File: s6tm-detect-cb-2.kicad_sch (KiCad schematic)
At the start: 51 parts, among them J1 USB_C_Receptacle_USB2.0_14P, J5 Conn_01x04_Pin, J8 Conn_01x04, SW1 SW_Push, SW2 SW_Push, SW3 SW_Push, U2 SN65HVD230, U3 ESP32-S3FN8, U7 NextPM, Y1 48M

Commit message: schem: add m3 mounting holes
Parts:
- added H5, H6, H7: MountingHole_Pad, MountingHole:MountingHole_3.2mm_M3_Pad_Via, symbol Mechanical:MountingHole_Pad
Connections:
- net GND: now also H5.1, H6.1, H7.1
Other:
- note added: "Mounting"

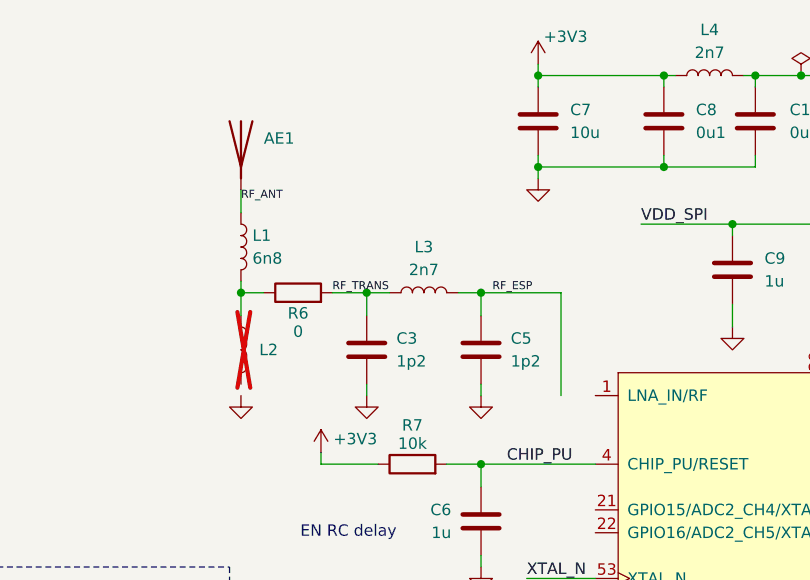
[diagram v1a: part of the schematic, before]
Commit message: schem: switch to external rf antenna
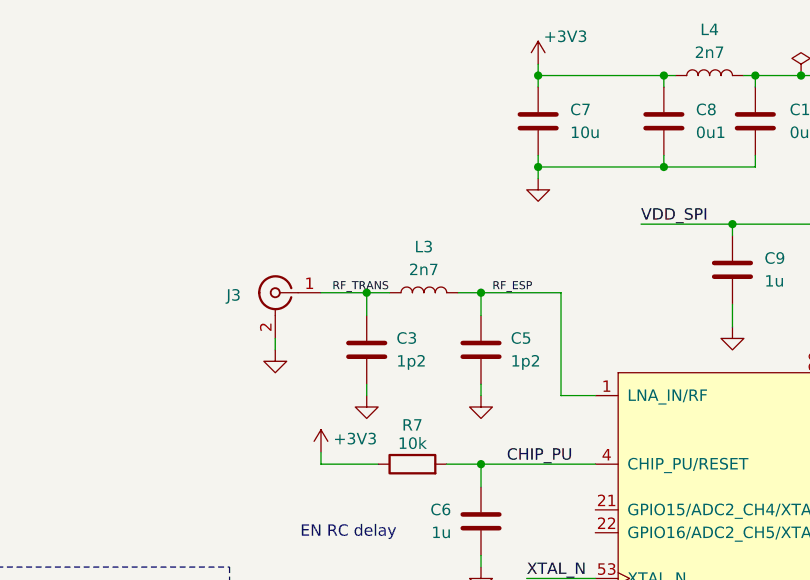
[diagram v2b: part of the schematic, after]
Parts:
- removed AE1: Antenna, RF_Antenna:Johanson_2450AT18x100, symbol Device:Antenna
- removed L1: 6n8, Inductor_SMD:L_0402_1005Metric, symbol Device:L
- removed L2: L, Inductor_SMD:L_0402_1005Metric, symbol Device:L
- removed R6: 0, Resistor_SMD:R_0402_1005Metric, symbol Device:R
- added J3: Conn_Coaxial, Connector_Coaxial:SMA_BAT_Wireless_BWSMA-KWE-Z001, symbol Connector:Conn_Coaxial
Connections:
- net GND: now also J3.2 (Ext)
- net RF_ESP: now also U3.1 (LNA_IN/RF)
- net RF_TRANS: now also J3.1 (In)

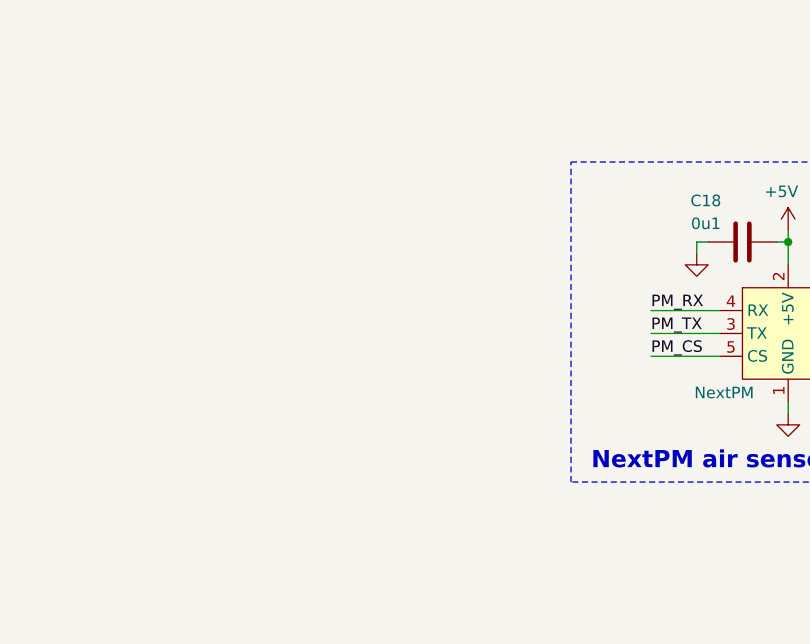
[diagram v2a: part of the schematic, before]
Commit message: schem: add htu21 h/t sensor
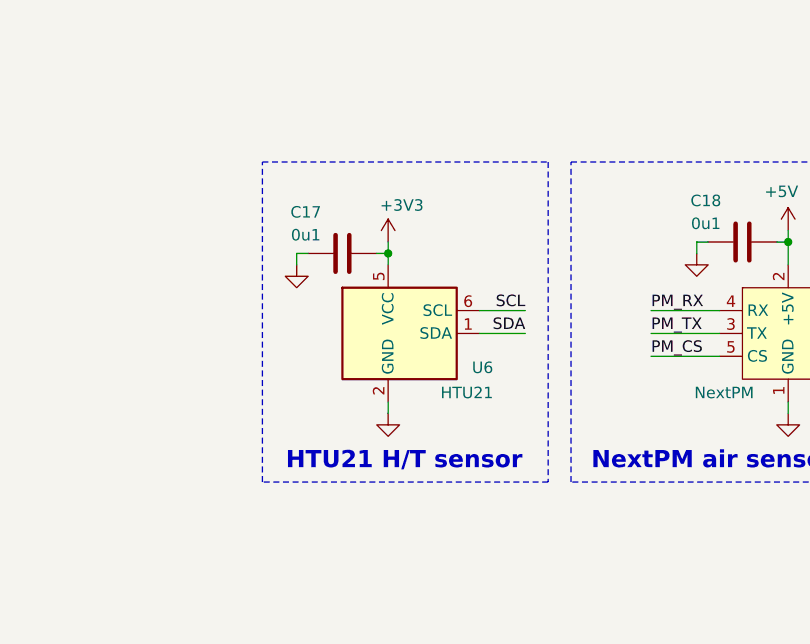
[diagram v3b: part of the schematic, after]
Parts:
- added C17: 0u1, Capacitor_SMD:C_0402_1005Metric, symbol Device:C
- added U6: HTU21, Package_SON:Texas_PWSON-N6, symbol Sensor_Humidity:HDC1080
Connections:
- net +3V3: now also C17.2, U6.5 (VCC)
- net GND: now also C17.1, U6.2 (GND)
- new net SCL: U6.6 (SCL)
- new net SDA: U6.1 (SDA)
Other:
- note added: "HTU21 H/T sensor"

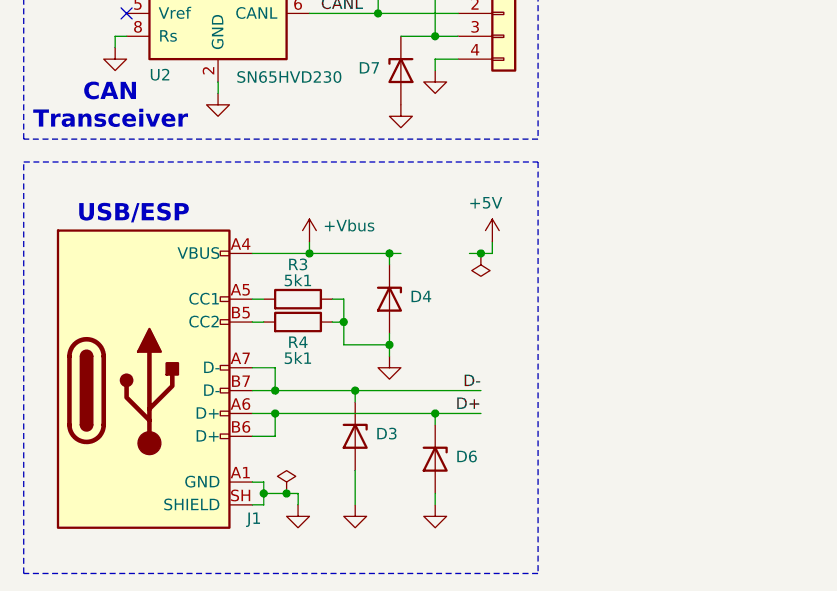
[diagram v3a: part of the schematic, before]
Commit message: schem: add MAX40203 ideal diode
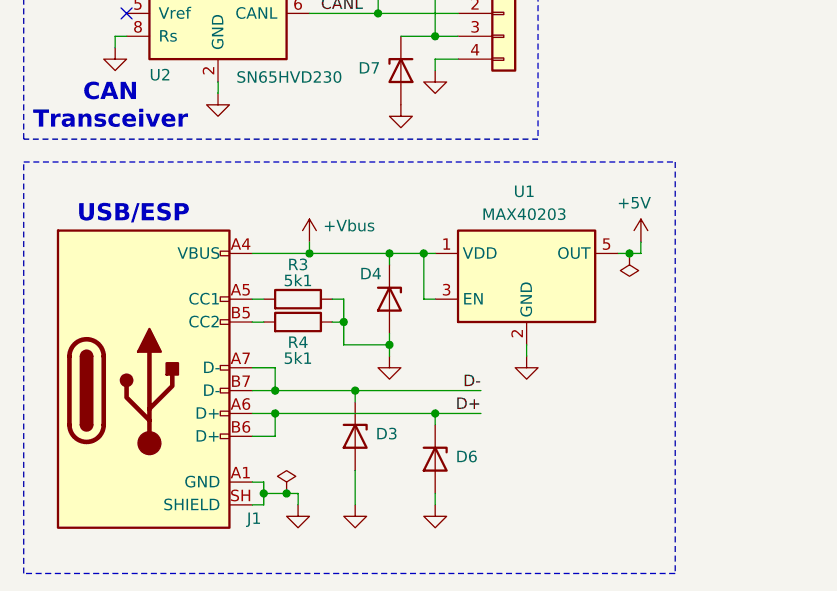
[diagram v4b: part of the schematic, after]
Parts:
- added U1: MAX40203, Package_TO_SOT_SMD:SOT-23-5, symbol Analog_Switch:MAX40200AUK
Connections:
- net +5V: now also U1.5 (OUT)
- net +Vbus: now also U1.1 (VDD), U1.3 (EN)
- net GND: now also U1.2 (GND)

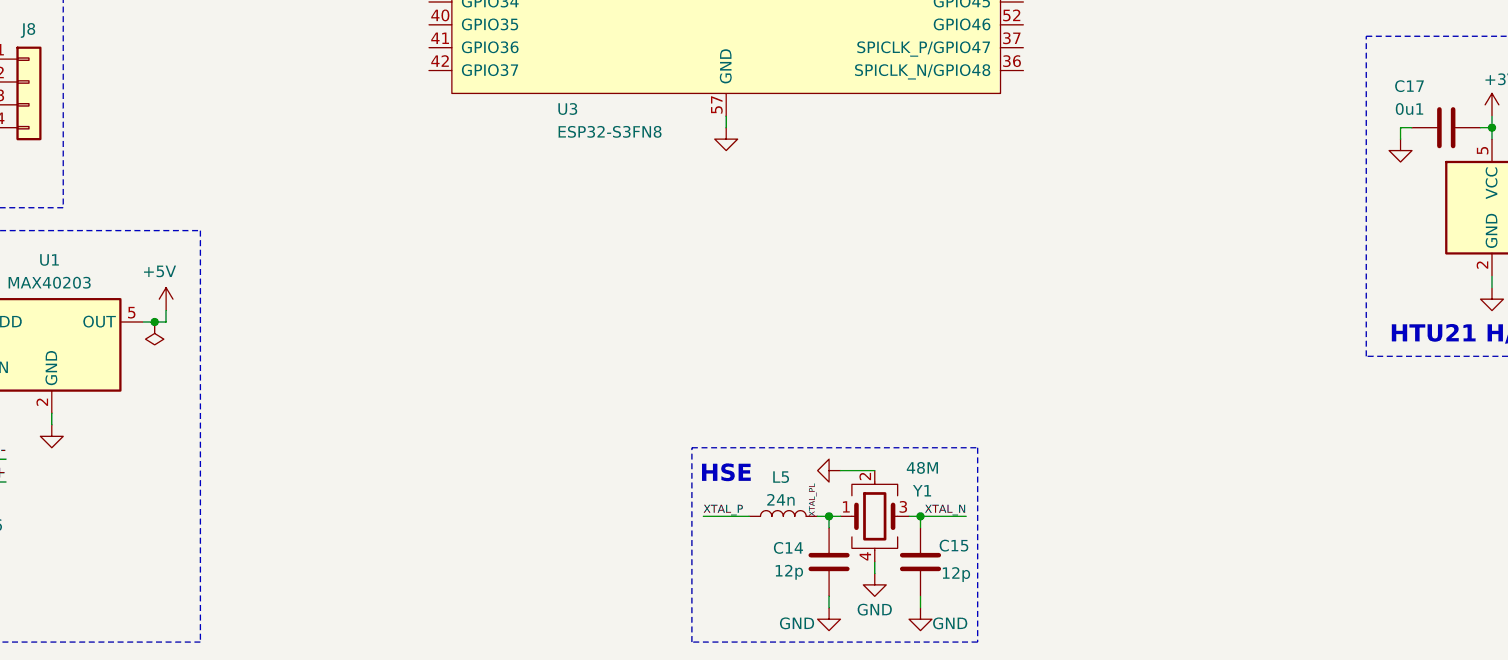
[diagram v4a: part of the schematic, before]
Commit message: schem: add TPS6282 3.3v SMPS
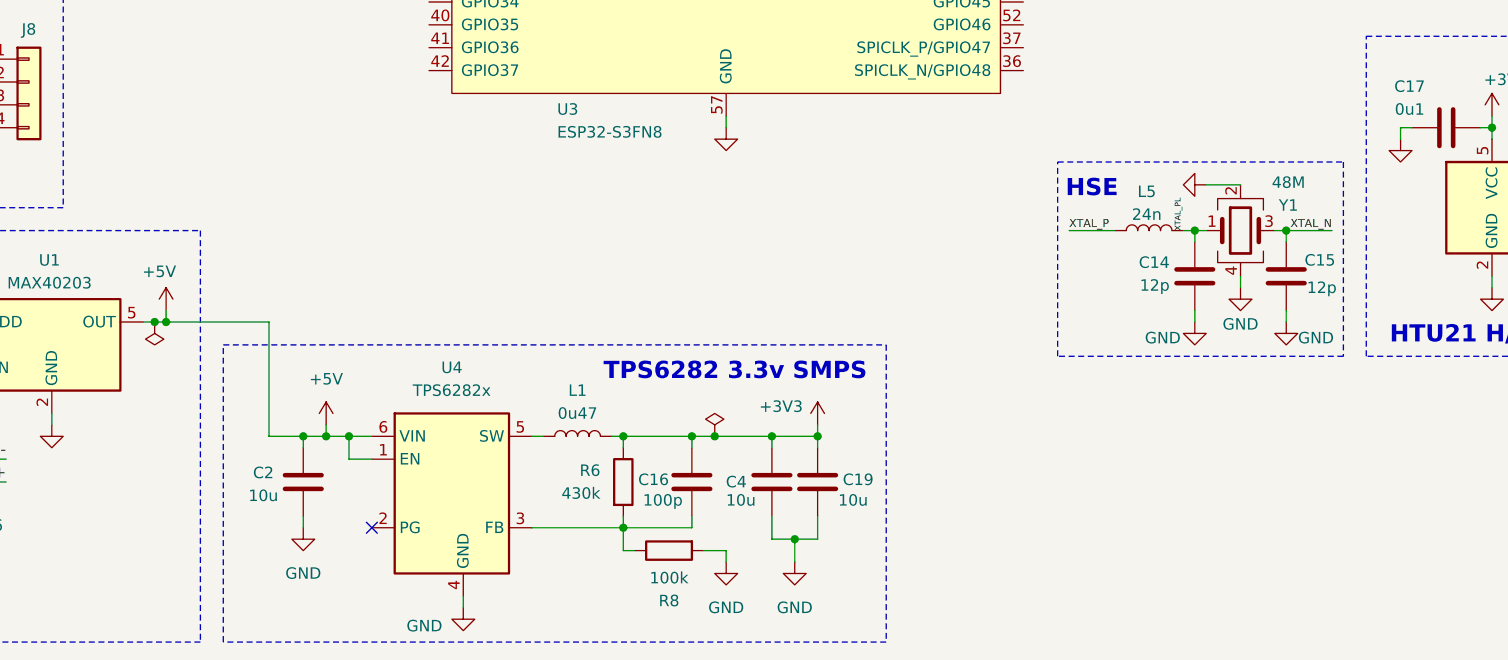
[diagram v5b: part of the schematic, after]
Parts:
- added C16: 100p, Capacitor_SMD:C_0402_1005Metric, symbol Device:C
- added C19, C4: 10u, Capacitor_SMD:C_0402_1005Metric, symbol Device:C
- added C2: 10u, Capacitor_SMD:C_0603_1608Metric, symbol Device:C
- added L1: 0u47, Pers:TDK_TFM201610ALC, symbol Device:L
- added R6: 430k, Resistor_SMD:R_0603_1608Metric, symbol Device:R
- added R8: 100k, Resistor_SMD:R_0402_1005Metric, symbol Device:R
- added U4: TPS6282x, Pers:Texas_VSON-6_1.5x1.5mm_P0.5mm_DMQ0006A, symbol Pers:TPS6282x
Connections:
- net +3V3: now also C16.1, C19.1, C4.1, L1.2, R6.1
- net +5V: now also C2.1, U4.1 (EN), U4.6 (VIN)
- net GND: now also C19.2, C2.2, C4.2, R8.2, U4.4 (GND)
- new net: C16.2, R6.2, R8.1, U4.3 (FB)
- new net: L1.1, U4.5 (SW)
- no-connect marks 2 -> 3
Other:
- note added: "TPS6282 3.3v SMPS"
- moved on the sheet: C14, C15, L5, Y1

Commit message: schem: update smps L part number
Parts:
- L1: JLCPCB Part # C2045043 -> C89446; Manufacturer Part Number TFM201610ALC-R47MTAA -> TFM201610GHM-R47MTAA
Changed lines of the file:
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@@
 			)
 		)
-		(property "JLCPCB Part #" "C2045043"
+		(property "JLCPCB Part #" "C89446"
 			(at 129.54 172.72 90)
 			(hide yes)
@@
 			)
 		)
-		(property "Manufacturer Part Number" "TFM201610ALC-R47MTAA"
+		(property "Manufacturer Part Number" "TFM201610GHM-R47MTAA"
 			(at 129.54 172.72 90)
 			(hide yes)

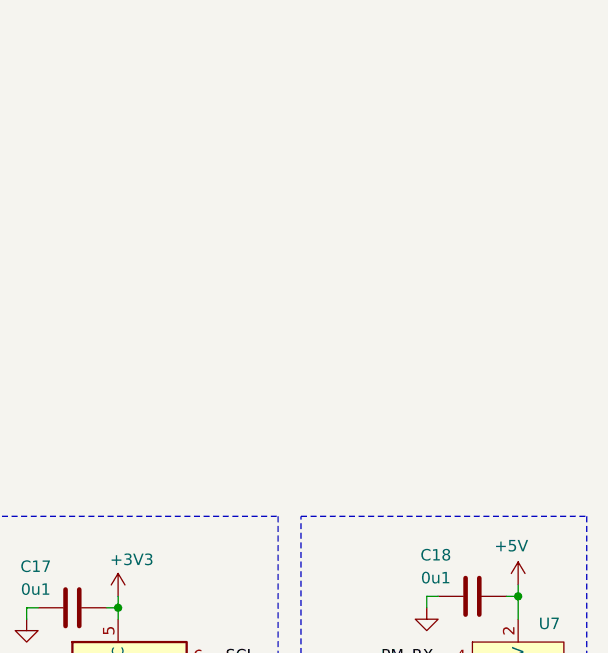
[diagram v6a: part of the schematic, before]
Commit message: schem: add ST7789 TFT connector
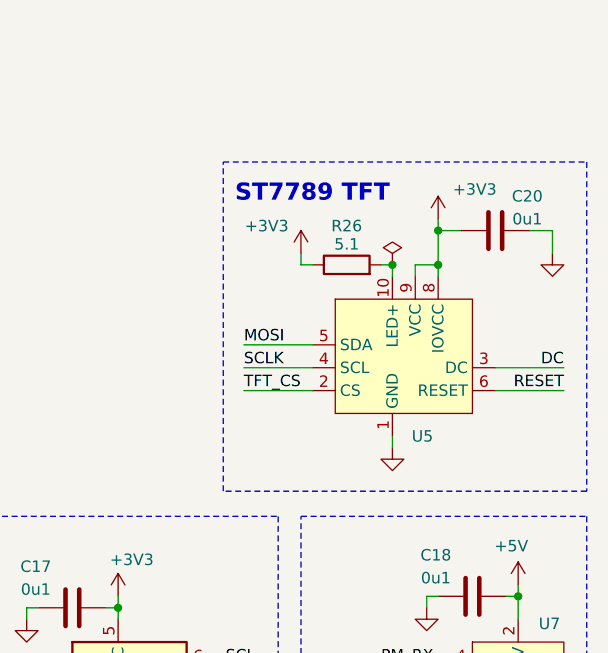
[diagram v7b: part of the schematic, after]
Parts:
- added C20: 0u1, Capacitor_SMD:C_0402_1005Metric, symbol Device:C
- added R26: 5.1, Resistor_SMD:R_0603_1608Metric, symbol Device:R
- added U5: (no value), Connector_FFC-FPC:Hirose_FH12-12S-0.5SH_1x12-1MP_P0.50mm_Horizontal, symbol GLCS:HS20HS072RX
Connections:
- net +3V3: now also C20.2, R26.1, U5.8 (IOVCC), U5.9 (VCC)
- net GND: now also C20.1, U5.1 (GND), U5.11 (LED-), U5.12 (GND), U5.MP (GND)
- new net: R26.2, U5.10 (LED+)
- new net DC: U5.3 (DC)
- new net MOSI: U5.5 (SDA)
- new net RESET: U5.6 (RESET)
- new net SCLK: U5.4 (SCL)
- new net TFT_CS: U5.2 (CS)
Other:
- note added: "ST7789 TFT"

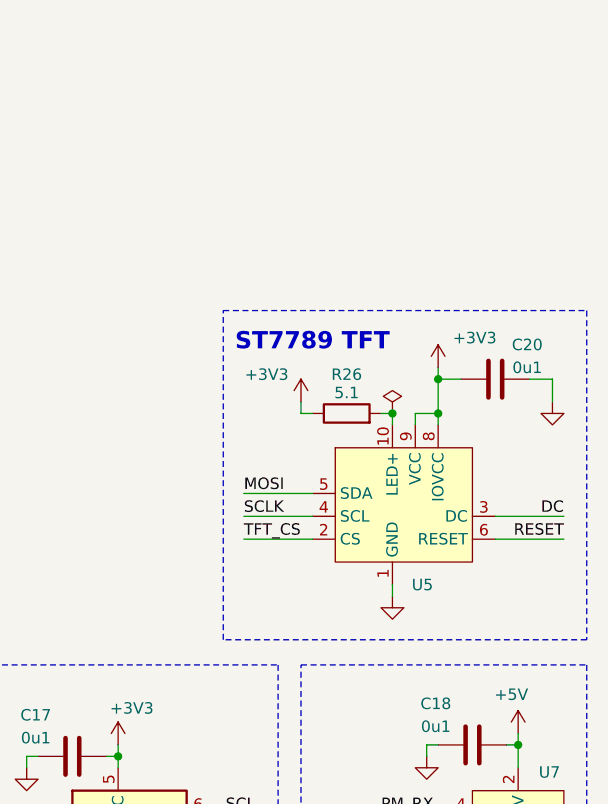
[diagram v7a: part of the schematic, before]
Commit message: schem: add tft dimming circuit
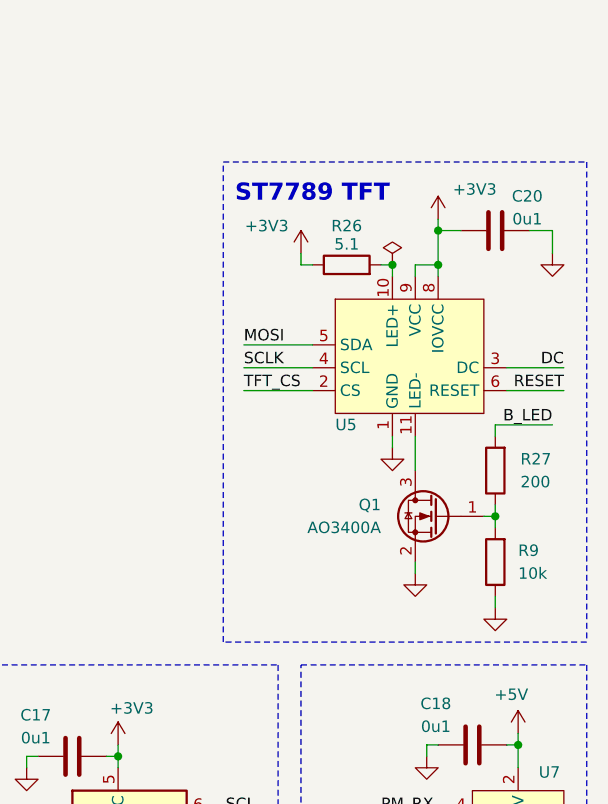
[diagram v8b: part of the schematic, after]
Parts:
- added Q1: AO3400A, Package_TO_SOT_SMD:SOT-23, symbol Transistor_FET:AO3400A
- added R27: 200, Resistor_SMD:R_0603_1608Metric, symbol Device:R
- added R9: 10k, Resistor_SMD:R_0402_1005Metric, symbol Device:R
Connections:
- net GND: now also Q1.2 (S), R9.1; no longer U5.11 (LED-)
- new net: Q1.3 (D), U5.11 (LED-)
- new net: Q1.1 (G), R27.1, R9.2
- new net B_LED: R27.2
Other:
- moved on the sheet: C20, R26
